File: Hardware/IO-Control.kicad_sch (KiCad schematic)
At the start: 40 parts, among them Q2 MMBT3904, SW1 RESET, U8 CH340G, U9 ESP32-PICO-MINI-02, Y1 12MHz

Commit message: LED driver part values & labels on IO page
Added the values (and some part numbers) for the LED drivers, and added some floating labels on the IO sheet to remind what still needs connecting.
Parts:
- added C27: 100n, symbol Device:C
- added C28: (no value), symbol Device:C
- C26: value (none) -> 10u
- D6: value (none) -> SS34
- F1: value (none) -> 0ZCJ0050FF2G; footprint (none) -> Fuse:Fuse_1206_3216Metric_Pad1.42x1.75mm_HandSolder
- J1: value (none) -> Molex 047053-1000
- J2: renamed from J?; value (none) -> S3B-XH-A
- P6: value (none) -> TYPE-C-31-M-12
- Q1, Q4: value (none) -> MMBT3904; footprint (none) -> Package_TO_SOT_SMD:SOT-23
- Q3: value (none) -> PMV16XNR; footprint (none) -> Package_TO_SOT_SMD:SOT-23_Handsoldering
- R19, R30: value (none) -> 4k7
- R20: value (none) -> 3k3
- R22, R23: value (none) -> 0R
- R24, R25, R28: value (none) -> 10k
- R26: value (none) -> 2k7
- R27: value (none) -> 1k
- R29: value (none) -> NF
- R31: renamed from R?; value (none) -> 4k7
- SW2: value (none) -> FLASH
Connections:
- net +12V: now also C27.1, C28.1
- net GND: now also C27.2, C28.2

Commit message: Most part assignents made, pending switch footprint & xtal selection
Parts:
- C18, C19: value 22p -> (none)
- C20, C22, C24, C25, C27: value 100n -> (none); Part_number (none) -> AC0805KRX7R7BB104
- C21: value 1u -> (none)
- C23: value 22u -> (none); Part_number (none) -> CL21A226MAYNNNE
- C26: value 10u -> (none); Part_number (none) -> CL21A106KAYNNNE
- D6: value SS34 -> (none); Part_number (none) -> SS34
- D7: value GREEN -> (none)
- D8: value RED -> (none)
- F1: value 0ZCJ0050FF2G -> (none); footprint Fuse:Fuse_1206_3216Metric_Pad1.42x1.75mm_HandSolder -> (none); Part_number (none) -> 0ZCJ0050FF2G
- J1: value Molex 047053-1000 -> (none); Part_number (none) -> 470531000
- J2: value S3B-XH-A -> (none); Part_number (none) -> S3B-XH-A
- P6: value TYPE-C-31-M-12 -> (none)
- Q1, Q2, Q4: value MMBT3904 -> (none); footprint Package_TO_SOT_SMD:SOT-23 -> (none); Part_number (none) -> MMBT3904
- Q3: value PMV16XNR -> (none); footprint Package_TO_SOT_SMD:SOT-23_Handsoldering -> (none); Part_number (none) -> PMV16XNR
- R17, R18: value 5k1 -> (none)
- R19, R30, R31: value 4k7 -> (none)
- R20: value 3k3 -> (none)
- R21, R24, R25, R28: value 10k -> (none)
- R22, R23: value 0R -> (none)
- R26: value 2k7 -> (none)
- R27: value 1k -> (none)
- R29: value NF -> (none)
- SW1: value RESET -> (none)
- SW2: value FLASH -> (none)
- U8: value CH340G -> (none); footprint Package_SO:SOIC-16_3.9x9.9mm_P1.27mm -> (none)
- U9: value ESP32-PICO-MINI-02 -> (none); footprint Package_DFN_QFN:QFN-48-1EP_7x7mm_P0.5mm_EP5.3x5.3mm -> (none)
- Y1: value 12MHz -> (none)

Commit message: Xtal footprint selected. Remaining parts need new footprints.
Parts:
- C18, C19: value (none) -> 22p; footprint (none) -> Capacitor_SMD:C_0805_2012Metric_Pad1.18x1.45mm_HandSolder
- C20, C22, C24, C25, C27: value (none) -> 100n; footprint (none) -> Capacitor_SMD:C_0805_2012Metric_Pad1.18x1.45mm_HandSolder
- C21, C28: value (none) -> 1u; footprint (none) -> Capacitor_SMD:C_0805_2012Metric_Pad1.18x1.45mm_HandSolder
- C23: value (none) -> 22u; footprint (none) -> Capacitor_SMD:C_0805_2012Metric_Pad1.18x1.45mm_HandSolder
- C26: value (none) -> 10u 25V; footprint (none) -> Capacitor_SMD:C_0805_2012Metric_Pad1.18x1.45mm_HandSolder
- D6: value (none) -> SS34; footprint (none) -> Diode_SMD:D_SMA_Handsoldering
- D7: value (none) -> GREEN; footprint (none) -> LED_SMD:LED_0603_1608Metric_Pad1.05x0.95mm_HandSolder
- D8: value (none) -> RED; footprint (none) -> LED_SMD:LED_0603_1608Metric_Pad1.05x0.95mm_HandSolder
- F1: value (none) -> 0ZCJ0050FF2G; footprint (none) -> Fuse:Fuse_1206_3216Metric_Pad1.42x1.75mm_HandSolder
- J1: value (none) -> Molex 047053-1000; footprint (none) -> Connector_Molex:Molex_KK-254_AE-6410-04A_1x04_P2.54mm_Vertical
- J2: value (none) -> S3B-XH-A; footprint (none) -> Connector_JST:JST_XH_S3B-XH-A-1_1x03_P2.50mm_Horizontal
- P6: value (none) -> TYPE-C-31-M-12
- Q1, Q2, Q4: value (none) -> MMBT3904; footprint (none) -> Package_TO_SOT_SMD:SOT-23
- Q3: value (none) -> PMV16XNR; footprint (none) -> Package_TO_SOT_SMD:SOT-23_Handsoldering
- R17, R18: value (none) -> 5k1; footprint (none) -> Resistor_SMD:R_0603_1608Metric_Pad0.98x0.95mm_HandSolder
- R19, R30, R31: value (none) -> 4k7; footprint (none) -> Resistor_SMD:R_0603_1608Metric_Pad0.98x0.95mm_HandSolder
- R20: value (none) -> 3k3; footprint (none) -> Resistor_SMD:R_0603_1608Metric_Pad0.98x0.95mm_HandSolder
- R21, R24, R25, R28: value (none) -> 10k; footprint (none) -> Resistor_SMD:R_0603_1608Metric_Pad0.98x0.95mm_HandSolder
- R22, R23: value (none) -> 0R; footprint (none) -> Resistor_SMD:R_0603_1608Metric_Pad0.98x0.95mm_HandSolder
- R26: value (none) -> 2k7; footprint (none) -> Resistor_SMD:R_0603_1608Metric_Pad0.98x0.95mm_HandSolder
- R27: value (none) -> 1k; footprint (none) -> Resistor_SMD:R_0603_1608Metric_Pad0.98x0.95mm_HandSolder
- R29: value (none) -> NF; footprint (none) -> Resistor_SMD:R_0603_1608Metric_Pad0.98x0.95mm_HandSolder
- SW1: value (none) -> RESET
- SW2: value (none) -> FLASH
- U8: value (none) -> CH340G; footprint (none) -> Package_SO:SOIC-16_3.9x9.9mm_P1.27mm
- U9: value (none) -> ESP32-PICO-MINI-02; footprint (none) -> Package_DFN_QFN:QFN-48-1EP_7x7mm_P0.5mm_EP5.3x5.3mm
- Y1: symbol Device:Crystal -> Device:Crystal_GND24; Part_number (none) -> TAXM12M4RLBDDT2T
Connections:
- net GND: now also Y1.2, Y1.4
- net at C19.1, U8.8 (XO): now also Y1.3; no longer Y1.2
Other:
- moved on the sheet: C18

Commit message: USB footprint added, mount holes added.
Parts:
- C18, C19: value 22p -> (none); footprint Capacitor_SMD:C_0805_2012Metric_Pad1.18x1.45mm_HandSolder -> (none)
- C20, C22, C24, C25, C27: value 100n -> (none); footprint Capacitor_SMD:C_0805_2012Metric_Pad1.18x1.45mm_HandSolder -> (none)
- C21, C28: value 1u -> (none); footprint Capacitor_SMD:C_0805_2012Metric_Pad1.18x1.45mm_HandSolder -> (none)
- C23: value 22u -> (none); footprint Capacitor_SMD:C_0805_2012Metric_Pad1.18x1.45mm_HandSolder -> (none)
- C26: value 10u 25V -> (none); footprint Capacitor_SMD:C_0805_2012Metric_Pad1.18x1.45mm_HandSolder -> (none)
- D6: value SS34 -> (none); footprint Diode_SMD:D_SMA_Handsoldering -> (none)
- D7: value GREEN -> (none); footprint LED_SMD:LED_0603_1608Metric_Pad1.05x0.95mm_HandSolder -> (none)
- D8: value RED -> (none); footprint LED_SMD:LED_0603_1608Metric_Pad1.05x0.95mm_HandSolder -> (none)
- F1: value 0ZCJ0050FF2G -> (none); footprint Fuse:Fuse_1206_3216Metric_Pad1.42x1.75mm_HandSolder -> (none)
- J1: value Molex 047053-1000 -> (none); footprint Connector_Molex:Molex_KK-254_AE-6410-04A_1x04_P2.54mm_Vertical -> (none)
- J2: value S3B-XH-A -> (none); footprint Connector_JST:JST_XH_S3B-XH-A-1_1x03_P2.50mm_Horizontal -> (none)
- P6: value TYPE-C-31-M-12 -> (none)
- Q1, Q2, Q4: value MMBT3904 -> (none); footprint Package_TO_SOT_SMD:SOT-23 -> (none)
- Q3: value PMV16XNR -> (none); footprint Package_TO_SOT_SMD:SOT-23_Handsoldering -> (none)
- R17, R18: value 5k1 -> (none); footprint Resistor_SMD:R_0603_1608Metric_Pad0.98x0.95mm_HandSolder -> (none)
- R19, R30, R31: value 4k7 -> (none); footprint Resistor_SMD:R_0603_1608Metric_Pad0.98x0.95mm_HandSolder -> (none)
- R20: value 3k3 -> (none); footprint Resistor_SMD:R_0603_1608Metric_Pad0.98x0.95mm_HandSolder -> (none)
- R21, R24, R25, R28: value 10k -> (none); footprint Resistor_SMD:R_0603_1608Metric_Pad0.98x0.95mm_HandSolder -> (none)
- R22, R23: value 0R -> (none); footprint Resistor_SMD:R_0603_1608Metric_Pad0.98x0.95mm_HandSolder -> (none)
- R26: value 2k7 -> (none); footprint Resistor_SMD:R_0603_1608Metric_Pad0.98x0.95mm_HandSolder -> (none)
- R27: value 1k -> (none); footprint Resistor_SMD:R_0603_1608Metric_Pad0.98x0.95mm_HandSolder -> (none)
- R29: value NF -> (none); footprint Resistor_SMD:R_0603_1608Metric_Pad0.98x0.95mm_HandSolder -> (none)
- SW1: value RESET -> (none)
- SW2: value FLASH -> (none)
- U8: value CH340G -> (none); footprint Package_SO:SOIC-16_3.9x9.9mm_P1.27mm -> (none)
- U9: value ESP32-PICO-MINI-02 -> (none); footprint Package_DFN_QFN:QFN-48-1EP_7x7mm_P0.5mm_EP5.3x5.3mm -> (none)

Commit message: Layout changes
Changed XT60 outputs to Mini-Fit Jr., laid out 80mm fan edge cuts, started positioning conns
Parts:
- C18, C19: value (none) -> 22p; footprint (none) -> Capacitor_SMD:C_0805_2012Metric_Pad1.18x1.45mm_HandSolder
- C20, C22, C24, C25, C27: value (none) -> 100n; footprint (none) -> Capacitor_SMD:C_0805_2012Metric_Pad1.18x1.45mm_HandSolder
- C21, C28: value (none) -> 1u; footprint (none) -> Capacitor_SMD:C_0805_2012Metric_Pad1.18x1.45mm_HandSolder
- C23: value (none) -> 22u; footprint (none) -> Capacitor_SMD:C_0805_2012Metric_Pad1.18x1.45mm_HandSolder
- C26: value (none) -> 10u 25V; footprint (none) -> Capacitor_SMD:C_0805_2012Metric_Pad1.18x1.45mm_HandSolder
- D6: value (none) -> SS34; footprint (none) -> Diode_SMD:D_SMA_Handsoldering
- D7: value (none) -> GREEN; footprint (none) -> LED_SMD:LED_0603_1608Metric_Pad1.05x0.95mm_HandSolder
- D8: value (none) -> RED; footprint (none) -> LED_SMD:LED_0603_1608Metric_Pad1.05x0.95mm_HandSolder
- F1: value (none) -> 0ZCJ0050FF2G; footprint (none) -> Fuse:Fuse_1206_3216Metric_Pad1.42x1.75mm_HandSolder
- J1: value (none) -> Molex 047053-1000; footprint (none) -> Connector_Molex:Molex_KK-254_AE-6410-04A_1x04_P2.54mm_Vertical
- J2: value (none) -> S3B-XH-A; footprint (none) -> Connector_JST:JST_XH_S3B-XH-A-1_1x03_P2.50mm_Horizontal
- P6: value (none) -> TYPE-C-31-M-12; footprint (none) -> PersonalConnectors:Korean_HRO_Type-C-31-M-12
- Q1, Q2, Q4: value (none) -> MMBT3904; footprint (none) -> Package_TO_SOT_SMD:SOT-23
- Q3: value (none) -> PMV16XNR; footprint (none) -> Package_TO_SOT_SMD:SOT-23_Handsoldering
- R17, R18: value (none) -> 5k1; footprint (none) -> Resistor_SMD:R_0603_1608Metric_Pad0.98x0.95mm_HandSolder
- R19, R30, R31: value (none) -> 4k7; footprint (none) -> Resistor_SMD:R_0603_1608Metric_Pad0.98x0.95mm_HandSolder
- R20: value (none) -> 3k3; footprint (none) -> Resistor_SMD:R_0603_1608Metric_Pad0.98x0.95mm_HandSolder
- R21, R24, R25, R28: value (none) -> 10k; footprint (none) -> Resistor_SMD:R_0603_1608Metric_Pad0.98x0.95mm_HandSolder
- R22, R23: value (none) -> 0R; footprint (none) -> Resistor_SMD:R_0603_1608Metric_Pad0.98x0.95mm_HandSolder
- R26: value (none) -> 2k7; footprint (none) -> Resistor_SMD:R_0603_1608Metric_Pad0.98x0.95mm_HandSolder
- R27: value (none) -> 1k; footprint (none) -> Resistor_SMD:R_0603_1608Metric_Pad0.98x0.95mm_HandSolder
- R29: value (none) -> NF; footprint (none) -> Resistor_SMD:R_0603_1608Metric_Pad0.98x0.95mm_HandSolder
- SW1: value (none) -> RESET
- SW2: value (none) -> FLASH
- U8: value (none) -> CH340G; footprint (none) -> Package_SO:SOIC-16_3.9x9.9mm_P1.27mm
- U9: value (none) -> ESP32-PICO-MINI-02; footprint (none) -> Package_DFN_QFN:QFN-48-1EP_7x7mm_P0.5mm_EP5.3x5.3mm
- Y1: value (none) -> 12MHz; footprint (none) -> Crystal:Crystal_SMD_3225-4Pin_3.2x2.5mm

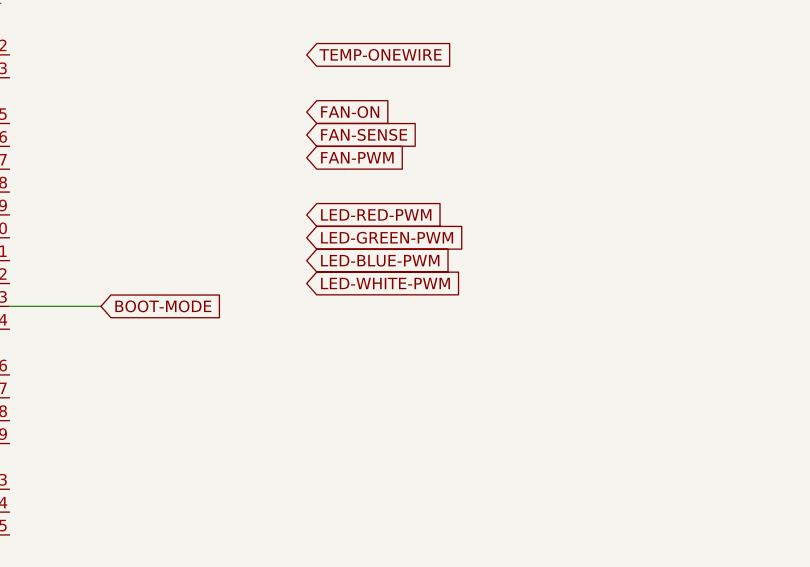
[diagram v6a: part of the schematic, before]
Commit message: removing white channel -- limited space on side of board from inductors
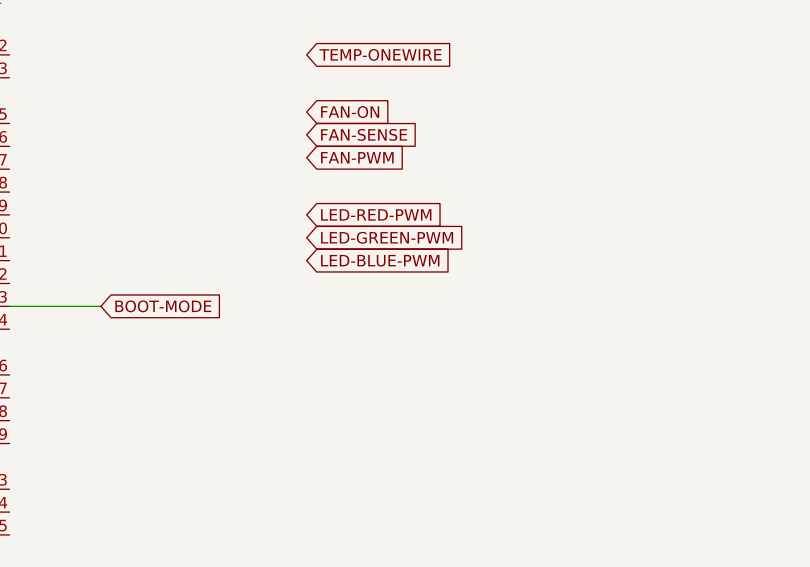
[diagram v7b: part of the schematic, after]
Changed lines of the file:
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@@
-    )
-  )
-  (global_label "LED-WHITE-PWM" (shape input) (at 227.33 175.26 0) (fields_autoplaced)
-    (effects (font (size 1.27 1.27)) (justify left))
-    (property "Intersheet References" "${INTERSHEET_REFS}" (id 0) (at 246.0112 175.1806 0)
-      (effects (font (size 1.27 1.27)) (justify left) hide)
     )
   )

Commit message: placement done, ESP32 footprint added
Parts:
- U9: footprint Package_DFN_QFN:QFN-48-1EP_7x7mm_P0.5mm_EP5.3x5.3mm -> PersonalDiscretes:ESP32-PICO-MINI-02
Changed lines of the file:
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@@
       (effects (font (size 1.27 1.27)) (justify left))
     )
-    (property "Footprint" "Package_DFN_QFN:QFN-48-1EP_7x7mm_P0.5mm_EP5.3x5.3mm" (id 2) (at 173.99 226.06 0)
+    (property "Footprint" "PersonalDiscretes:ESP32-PICO-MINI-02" (id 2) (at 173.99 226.06 0)
       (effects (font (size 1.27 1.27)) hide)
     )
